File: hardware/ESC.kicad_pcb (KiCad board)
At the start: 4 copper layers, 52 x 25 mm, 89 parts, among them J1 +, J10 +, J2 -, J3 +, J4 +, J5 +, J6 +, J7 Conn_01x03, J8 +, J9 +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

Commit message: made pcb layout
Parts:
- removed C10, C7: 100nF, Capacitor_SMD:C_0402_1005Metric
- removed C12, C13: 1uF, Capacitor_SMD:C_0402_1005Metric
- removed C14: 2.2uF, Capacitor_SMD:C_0603_1608Metric
- removed C8: 10uF, Capacitor_SMD:C_0603_1608Metric
- removed R10: 100K, Resistor_SMD:R_0402_1005Metric
- removed R11: 3.3K, Resistor_SMD:R_0402_1005Metric
- removed R12: 1K, Resistor_SMD:R_0402_1005Metric
- removed R14, R15: 10k, Resistor_SMD:R_0402_1005Metric
- removed SW3: SW_Push, Button_Switch_SMD:SW_Push_SPST_NO_Alps_SKRK
- removed U1: DRV8323RSRGZR, Package_DFN_QFN:QFN-48-1EP_7x7mm_P0.5mm_EP5.1x5.1mm_ThermalVias
- added C37: 10uF, Capacitor_SMD:C_0603_1608Metric, F.Cu at (143.4, 107.0)
- added C38: 15uF, Capacitor_SMD:C_0603_1608Metric, F.Cu at (140.2, 101.4)
- added C39: 15uF, Capacitor_SMD:C_0603_1608Metric, F.Cu at (140.2, 99.9)
- added C40: 100nF, Capacitor_SMD:C_0402_1005Metric, F.Cu at (140.2, 110.1)
- added C41: 100nF, Capacitor_SMD:C_0402_1005Metric, F.Cu at (168.2, 100.7)
- added C42: 1uF, Capacitor_SMD:C_0402_1005Metric, F.Cu at (163.4, 103.5)
- added C43: 100nF, Capacitor_SMD:C_0402_1005Metric, F.Cu at (166.9, 110.5)
- added R29: 28K, Resistor_SMD:R_0402_1005Metric, F.Cu at (142.2, 112.6)
- added R30: 8.45K, Resistor_SMD:R_0402_1005Metric, F.Cu at (144.1, 112.6)
- added R31: 10k, Resistor_SMD:R_0402_1005Metric, F.Cu at (168.2, 98.4)
- added R32: 100K, Resistor_SMD:R_0402_1005Metric, F.Cu at (165.1, 100.8)
- added R33: 10k, Resistor_SMD:R_0402_1005Metric, F.Cu at (155.3, 97.7)
- added TP1: TestPoint, TestPoint:TestPoint_Pad_1.5x1.5mm, B.Cu at (137.5, 113.3)
- added U3: LMR16006X, Package_TO_SOT_SMD:SOT-23-6, F.Cu at (142.6, 110.0)
- added U4: DRV8323SRTAR, ESC-footprints:DRV8323SRTAR, F.Cu at (167.6, 105.4)
- C11, D1, D2, FB1, JP1, R13, R20: moved to F.Cu
- C9: value 100nF -> 1uF; moved to F.Cu
- L1: value 22uH -> 27uH; footprint Inductor_SMD:L_APV_ANR6020 -> Inductor_SMD:L_APV_ANR4030; moved to F.Cu
- Q1, Q2, Q3, Q4, Q5, Q6: value AGM60P30AP -> AGM60P30A; footprint Package_DFN_QFN:PQFN-8-EP_6x5mm_P1.27mm_Generic -> Diode_SMD:D_QFN_3.3x3.3mm_P0.65mm; moved to F.Cu
- Q7: footprint Package_DFN_QFN:PQFN-8-EP_6x5mm_P1.27mm_Generic -> Diode_SMD:D_QFN_3.3x3.3mm_P0.65mm; moved to F.Cu
- R16, R18, R21, R22, R24, R26, R27: value 162K -> 226K
- R17, R19, R23, R25: value 20K -> 28K
- R28: value 10K -> 100K
- moved J10 27.7 mm to (153.3, 112.0)
- moved R28 22.0 mm to (144.8, 108.7), turned to -90 degrees
- moved C20 19.5 mm to (169.5, 89.8), turned to -90 degrees
- moved Q1 18.9 mm to (175.7, 108.5), turned to 0 degrees
- moved D1 16.2 mm to (138.3, 108.0), turned to 180 degrees
- moved C29 14.9 mm to (159.9, 110.3), turned to -90 degrees
- moved Q5 14.6 mm to (175.7, 91.3), turned to 0 degrees
- moved C9 14.4 mm to (166.9, 109.5)
- moved R13 13.7 mm to (142.5, 85.7)
- moved J9 13.6 mm to (142.4, 112.0), turned to 180 degrees
- moved C11 13.5 mm to (165.0, 109.5)
- moved C26 13.5 mm to (158.7, 110.2), turned to -90 degrees
- moved C32 12.3 mm to (144.1, 105.8), turned to 180 degrees
- moved C18 11.7 mm to (154.5, 90.0), turned to -90 degrees
- moved R25 11.4 mm to (144.1, 104.8), turned to 180 degrees
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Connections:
- net /BGND renamed Net-(D1-K)
- C9 pad 2: GND -> Net-(U4-VCP)
- R28 pad 1: /BOOT -> VBUS
- R28 pad 2: GND -> Net-(U3-~{SHDN})
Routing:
- net +3.3V: track 52.3 -> 0.00 mm, vias 6 -> 0
- net GND: track 48.8 -> 0.00 mm, vias 74 -> 0
- net /BEMF_A: track 42.7 -> 0.00 mm, vias 2 -> 0
- net /BEMF_B: track 41.5 -> 0.00 mm, vias 2 -> 0
- net /BEMF_C: track 38.6 -> 0.00 mm, vias 2 -> 0
- net VBUS: track 29.3 -> 0.00 mm, vias 64 -> 0
- net /RESET: track 26.6 -> 0.00 mm, vias 2 -> 0
- net /MOTOR_A: track 26.1 -> 0.00 mm, vias 1 -> 0
- net /DRV_EN: track 25.7 -> 0.00 mm, vias 2 -> 0
- net /GLA: track 23.9 -> 0.00 mm, vias 2 -> 0
- net /DRV_CAL: track 23.8 -> 0.00 mm, vias 2 -> 0
- net /FAULT: track 23.7 -> 0.00 mm, vias 2 -> 0
- net /SPA: track 22.5 -> 0.00 mm, vias 4 -> 0
- net /GLC: track 21.0 -> 0.00 mm, vias 2 -> 0
- net /MOTOR_C: track 20.2 -> 0.00 mm, vias 1 -> 0
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- removed copper zone on In2.Cu, net +3.3V
- removed copper zone on B.Cu, net /MOTOR_A
- removed copper zone on B.Cu, net /MOTOR_B
- removed copper zone on B.Cu, net /MOTOR_C
- removed copper zone on B.Cu, net /SPA
- removed copper zone on F.Cu, net /SPA
- removed copper zone on B.Cu, net /SPB
- removed copper zone on F.Cu, net /SPB
- removed copper zone on B.Cu, net /SPC
- removed copper zone on F.Cu, net /SPC
- removed copper zone on B.Cu, net GND
- removed copper zone on F.Cu, net GND
- removed copper zone on In1.Cu, net GND
- removed copper zone on B.Cu, net Net-(D2-A2)
- removed copper zone on B.Cu, net VBUS
- removed copper zone on F.Cu, net VBUS
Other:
- board size 52 x 25 mm -> 65 x 30 mm
- board text removed: "BOOT"
- board text removed: "CCW"
- board text removed: "CW"
- board text removed: "GND"
- board text removed: "RST"
- board text removed: "SWCLK"
- board text removed: "SWDIO"
- board text removed: "V1.0"

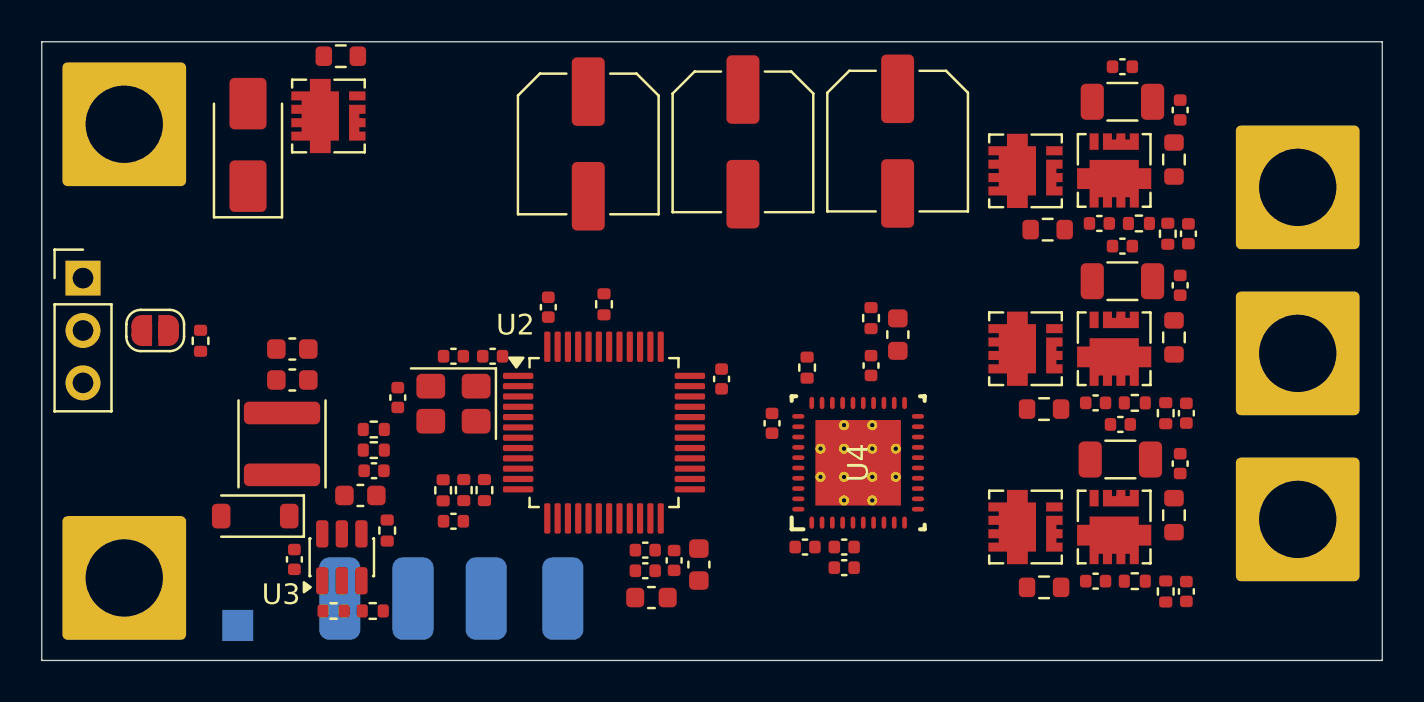
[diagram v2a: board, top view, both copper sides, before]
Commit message: added bulk capacitor
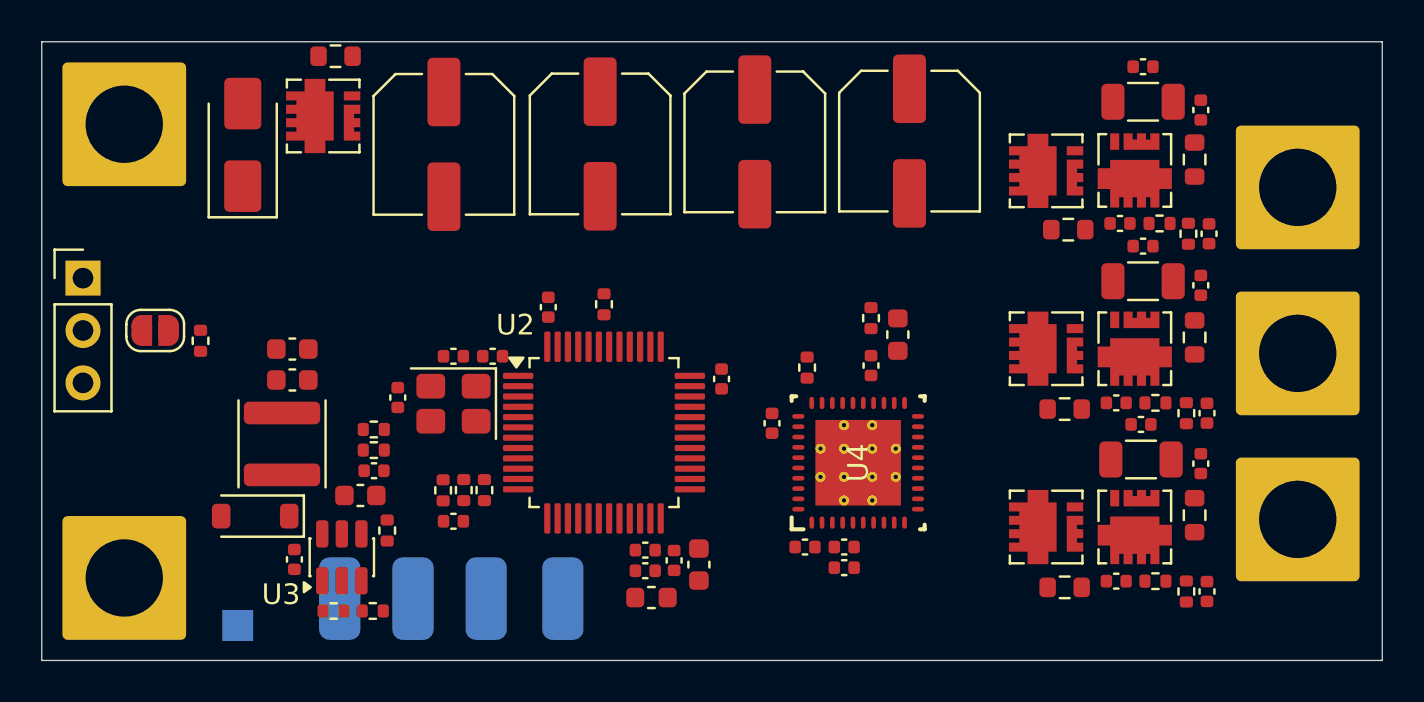
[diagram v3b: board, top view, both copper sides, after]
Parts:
- added C35: 100uF, Capacitor_SMD:C_Elec_6.3x7.7, F.Cu at (147.5, 90.0)
- moved C1 1.00 mm to (180.3, 93.8)
- moved C15 1.00 mm to (181.4, 86.2)
- moved C16 1.00 mm to (181.4, 94.9)
- moved C17 1.00 mm to (181.3, 103.6)
- moved C2 1.00 mm to (184.2, 88.3)
- moved C22 1.00 mm to (184.5, 103.0)
- moved C23 1.00 mm to (184.6, 94.3)
- moved C25 1.00 mm to (184.5, 111.7)
- moved C3 1.00 mm to (180.1, 102.5)
- moved C4 1.00 mm to (184.2, 96.8)
- moved C5 1.00 mm to (180.1, 111.2)
- moved C6 1.00 mm to (184.2, 105.5)
- moved Q1 1.00 mm to (176.7, 108.5)
- moved Q2 1.00 mm to (181.0, 91.2)
- moved Q3 1.00 mm to (176.7, 99.9)
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
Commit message: routed pcb
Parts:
- moved J6 18.2 mm to (188.9, 90.0)
- moved J4 17.9 mm to (188.9, 110.0)
- moved C15 17.3 mm to (181.4, 103.5)
- moved C17 17.3 mm to (181.3, 86.3), turned to 180 degrees
- moved C25 17.3 mm to (184.5, 94.4)
- moved C5 17.3 mm to (180.1, 93.9)
- moved Q2 17.3 mm to (181.0, 108.5)
- moved Q6 17.3 mm to (181.0, 91.2)
- moved R1 17.3 mm to (177.8, 111.4)
- moved R2 17.3 mm to (183.9, 108.0)
- moved R22 17.3 mm to (182.0, 93.9)
- moved R23 17.3 mm to (183.5, 94.4)
- moved R3 17.3 mm to (181.4, 105.2)
- moved C1 17.3 mm to (180.3, 111.1)
- moved C2 17.3 mm to (184.2, 105.6)
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- renumbered U4 to U1
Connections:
- U1 pad V: (no net) -> GND
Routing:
- net /BEMF_B: track 0.00 -> 50.3 mm, vias 0 -> 2
- net /BEMF_A: track 0.00 -> 48.0 mm, vias 0 -> 2
- net /BEMF_C: track 0.00 -> 45.5 mm, vias 0 -> 2
- net VBUS: track 0.00 -> 38.0 mm, vias 0 -> 2
- net +3.3V: track 0.00 -> 38.0 mm, vias 0 -> 9
- net GND: track 0.00 -> 37.5 mm, vias 0 -> 182
- net /SPC: track 0.00 -> 33.2 mm, vias 0 -> 2
- net /PWM_IN: track 0.00 -> 29.8 mm
- net /DIR: track 0.00 -> 29.5 mm
- net /SPB: track 0.00 -> 26.3 mm, vias 0 -> 2
- net /MOTOR_C: track 0.00 -> 24.5 mm, vias 0 -> 1
- net /SPA: track 0.00 -> 22.8 mm, vias 0 -> 2
- net /MOTOR_A: track 0.00 -> 22.3 mm, vias 0 -> 1
- net /GLC: track 0.00 -> 21.7 mm, vias 0 -> 2
- net /MOTOR_B: track 0.00 -> 21.0 mm, vias 0 -> 1
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- added copper zone on In2.Cu, net +3.3V
- added copper zone on F.Cu, net /MOTOR_A
- added copper zone on F.Cu, net /MOTOR_B
- added copper zone on F.Cu, net /MOTOR_C
- added copper zone on B.Cu, net GND
- added copper zone on F.Cu, net GND
- added copper zone on In1.Cu, net GND
- added copper zone on F.Cu, net Net-(D2-A2)
- added copper zone on F.Cu, net VBUS

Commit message: touched up pcb
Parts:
- removed R32: 100K, Resistor_SMD:R_0402_1005Metric
- Q1, Q2, Q3, Q4, Q5, Q6: value AGM60P30A -> AGM60P30AP
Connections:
- U1 pad 30: Net-(U4-ENABLE) -> /DRV_EN
- U2 pad 45: /BOOT -> unconnected-(U2-PB8-Pad45)
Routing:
- net /DRV_EN: track 0.00 -> 15.9 mm, vias 0 -> 2
- net Net-(U4-ENABLE): track 1.32 -> 0.00 mm
- net +3.3V: track 38.0 -> 37.0 mm
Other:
- board text added: "3.3v"
- board text added: "Closed:CCW"
- board text added: "GND"
- board text added: "Open:CW"
- board text added: "RESET"
- board text added: "SWCLK"
- board text added: "SWDIO"
